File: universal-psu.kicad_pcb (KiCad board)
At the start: 4 copper layers, 150 x 80 mm, 76 parts, among them J1 Screw_Terminal_01x04, J2 Screw_Terminal_01x04, J3 Screw_Terminal_01x04

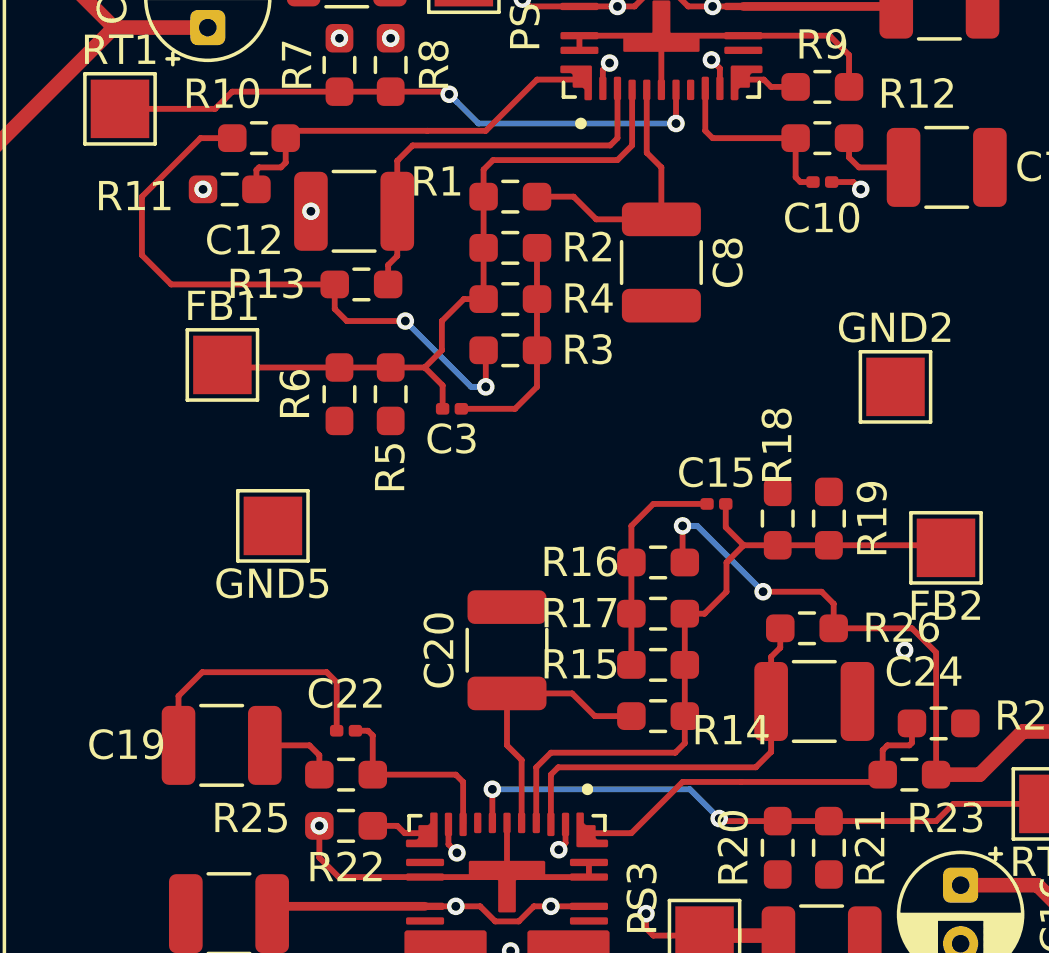
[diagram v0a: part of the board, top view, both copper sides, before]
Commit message: silkscreen and one part footprint and part number change for C3, C10, C15 and C22
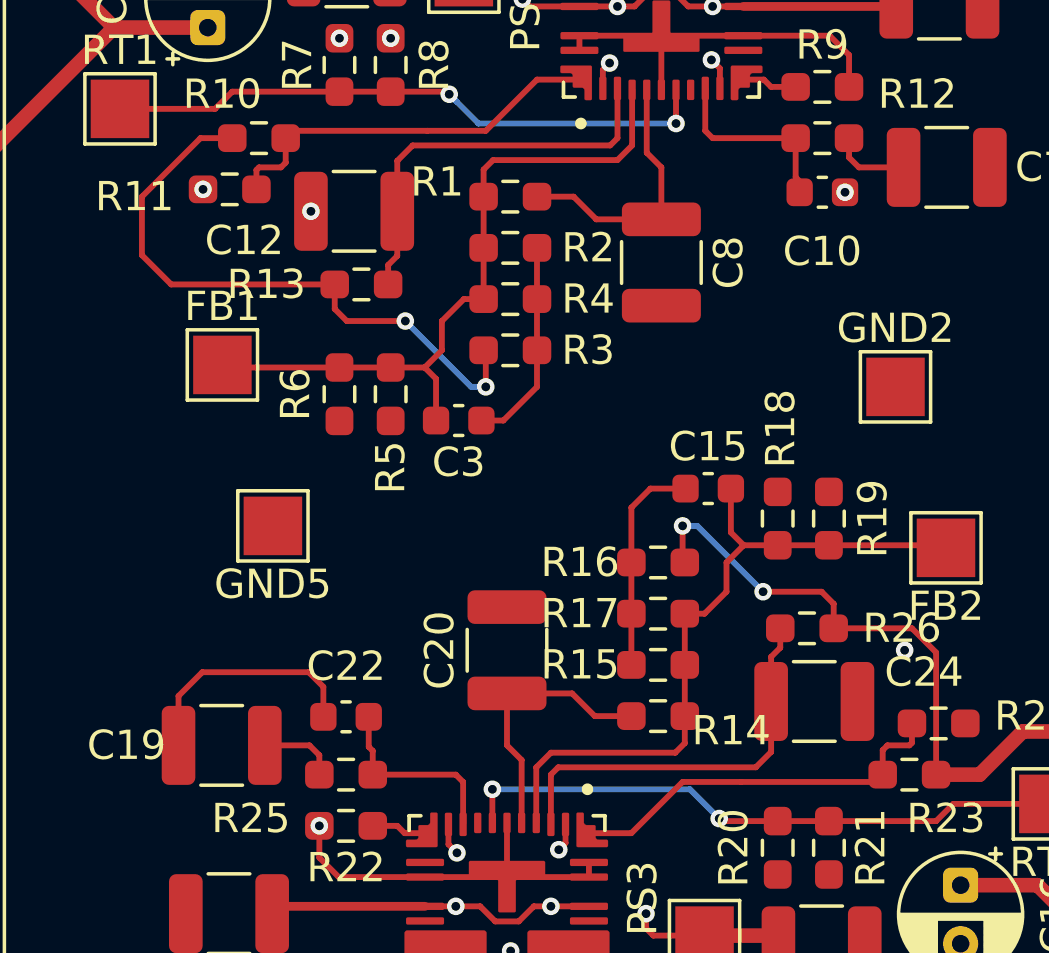
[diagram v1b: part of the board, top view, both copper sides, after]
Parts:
- C10, C15, C22, C3: footprint Capacitor_SMD:C_0201_0603Metric -> Capacitor_SMD:C_0603_1608Metric
- moved C15 0.59 mm to (132.2, 60.5)
- moved C22 0.47 mm to (119.9, 68.2)
- moved C3 0.46 mm to (123.7, 58.1)
- moved C10 0.35 mm to (136.2, 50.3)
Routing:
- net GND: track 36.1 -> 34.0 mm
- net Net-(C3-Pad1): track 7.65 -> 7.13 mm

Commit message: Connector change and silkscreen
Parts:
- added J4: Screw_Terminal_01x04, TerminalBlock_Phoenix:TerminalBlock_Phoenix_MKDS-1,5-4-5.08_1x04_P5.08mm_Horizontal, F.Cu at (66.6, 27.0)
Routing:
- net +12V: track 186.4 -> 269.4 mm
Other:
- board text added: "12V_OUT"
- board text added: "3V3_OUT"
- board text added: "5V_OUT"
- board text added: "AC_LIVE"
- board text added: "AC_RET"
- board text added: "GND"
